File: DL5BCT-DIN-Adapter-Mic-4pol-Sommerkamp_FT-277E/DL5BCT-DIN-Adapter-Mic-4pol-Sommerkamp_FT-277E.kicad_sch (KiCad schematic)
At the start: 2 parts, among them J1 DIN-5_180degree, J2 GX16-4_Radio_Microphone-4-pol

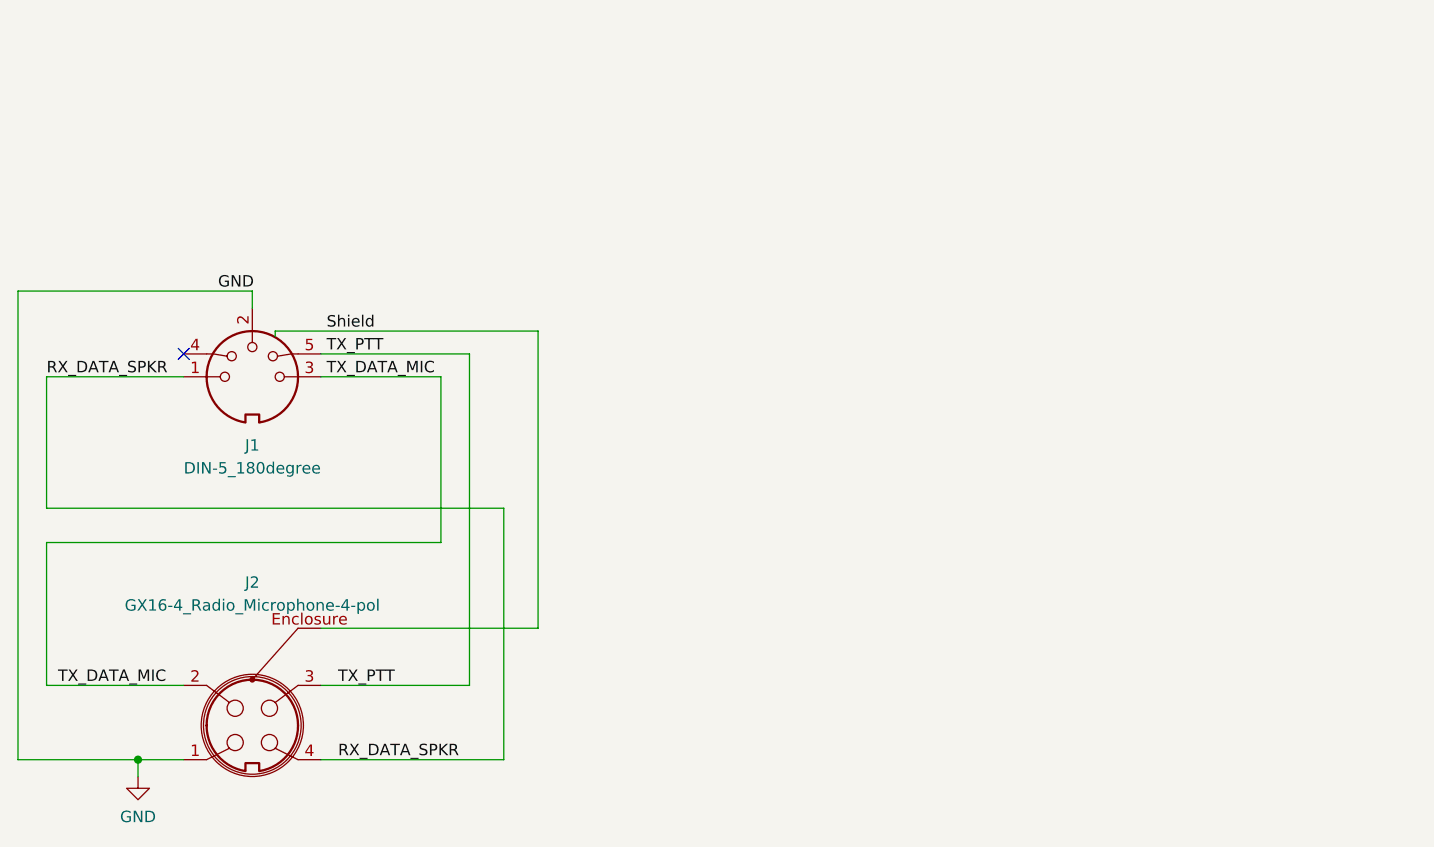
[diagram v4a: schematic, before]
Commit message: Added 'text table' with cable colour conventions. 	modified:   DL5BCT-DIN-Adapter-Mic-4pol-Sommerkamp_FT-277E/DL5BCT-DIN-Adapter-Mic-4pol-Sommerkamp_FT-277E.kicad_sch 	modified:   DL5BCT-DIN-Adapter-Mic-6pol-Kenwood_Trio_TR9000/DL5BCT-DIN-Adapter-Mic-6pol-Kenwood_Trio_TR9000.kicad_sch 	modified:   DL5BCT-DIN-Standard/DL5BCT-DIN-Standard.kicad_sch
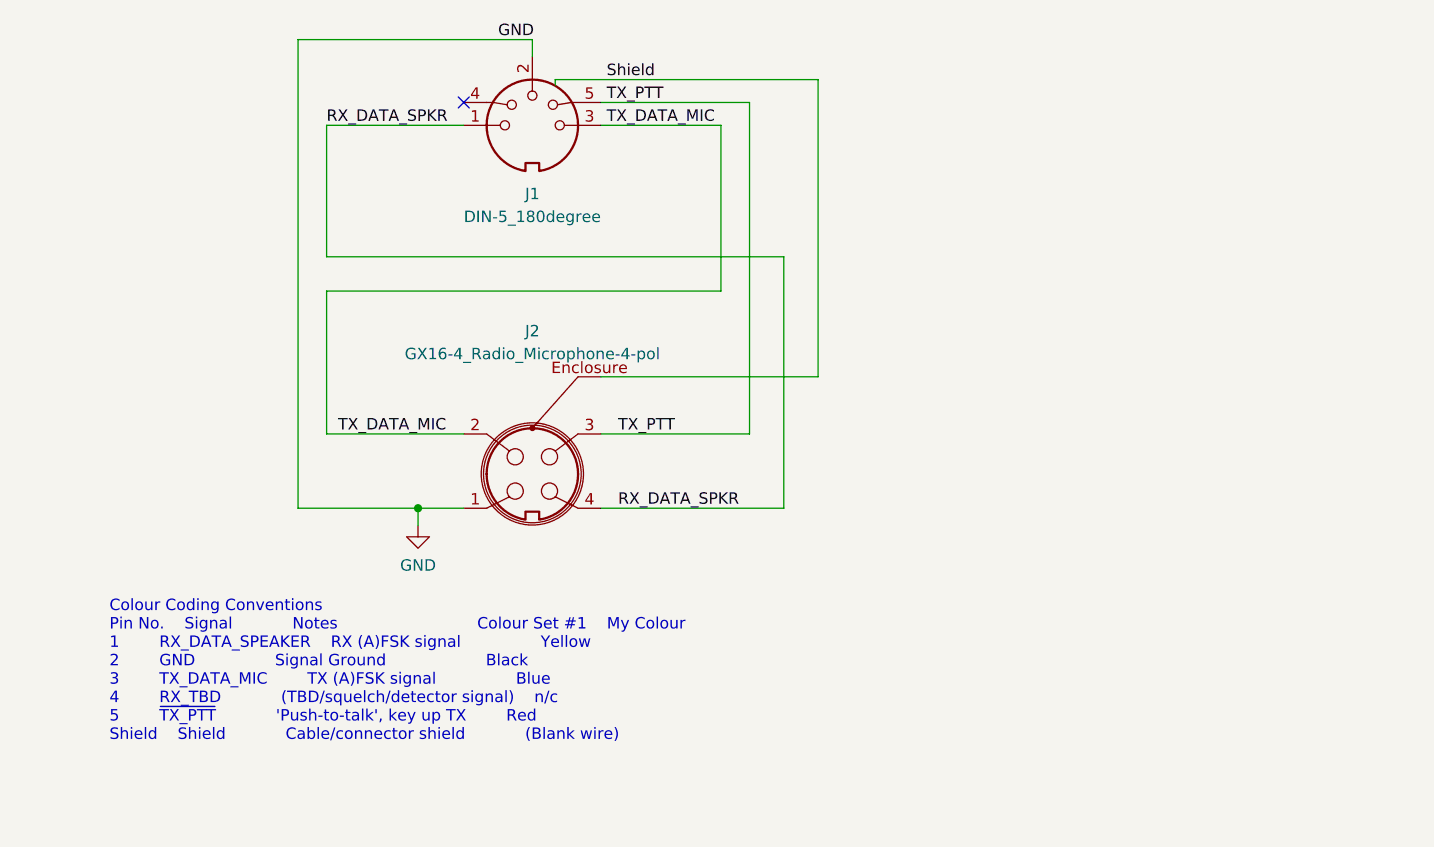
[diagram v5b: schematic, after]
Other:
- note added: "Colour Coding Conventions Pin No. Signal Notes Colour Set #1 My Colour 1 RX_DATA_SPEAKER RX (A)FSK signal Yellow 2 GND Signal Ground Black 3 TX_DATA_MIC TX (A)FSK signal Blue 4 RX_TBD (TBD/squelch/detector signal) n/c 5 ~{TX_PTT} 'Push-to-talk', key up TX Red Shield Shield Cable/connector shield (Blank wire)"
- moved on the sheet: J1, J2
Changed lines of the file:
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@@
 (kicad_sch (version 20211123) (generator eeschema)
-  (paper "A5" portrait)
+  (paper "A5")
   (title_block
     (title "Adaptor DL5BCT-DIN-Standard <--> TRX MIC 4-pol")
@@
     (comment 2 "Sommerkamp FT-277 E")
   )
-  (junction (at 62.865 100.965) (diameter 0) (color 0 0 0 0)
+  (junction (at 93.98 73.025) (diameter 0) (color 0 0 0 0)
   )
-  (no_connect (at 67.945 55.88))
-  (wire (pts (xy 52.705 73.025) (xy 52.705 58.42))
+  (no_connect (at 99.06 27.94))
+  (wire (pts (xy 83.82 45.085) (xy 83.82 30.48))
     (stroke (width 0) (type default) (color 0 0 0 0))
   )
-  (wire (pts (xy 96.52 76.835) (xy 96.52 58.42))
+  (wire (pts (xy 127.635 48.895) (xy 127.635 30.48))
     (stroke (width 0) (type default) (color 0 0 0 0))
   )
-  (wire (pts (xy 62.865 100.965) (xy 67.945 100.965))
+  (wire (pts (xy 93.98 73.025) (xy 99.06 73.025))
     (stroke (width 0) (type default) (color 0 0 0 0))
   )
-  (wire (pts (xy 78.105 53.34) (xy 78.105 53.975))
+  (wire (pts (xy 109.22 25.4) (xy 109.22 26.035))
     (stroke (width 0) (type default) (color 0 0 0 0))
   )
-  (wire (pts (xy 52.705 92.71) (xy 52.705 76.835))
+  (wire (pts (xy 83.82 64.77) (xy 83.82 48.895))
     (stroke (width 0) (type default) (color 0 0 0 0))
   )
-  (wire (pts (xy 52.705 76.835) (xy 96.52 76.835))
+  (wire (pts (xy 83.82 48.895) (xy 127.635 48.895))
     (stroke (width 0) (type default) (color 0 0 0 0))
   )
-  (wire (pts (xy 75.565 48.895) (xy 75.565 50.8))
+  (wire (pts (xy 106.68 20.955) (xy 106.68 22.86))
     (stroke (width 0) (type default) (color 0 0 0 0))
   )
-  (wire (pts (xy 83.185 86.36) (xy 107.315 86.36))
+  (wire (pts (xy 114.3 58.42) (xy 138.43 58.42))
     (stroke (width 0) (type default) (color 0 0 0 0))
   )
-  (wire (pts (xy 103.505 73.025) (xy 52.705 73.025))
+  (wire (pts (xy 134.62 45.085) (xy 83.82 45.085))
     (stroke (width 0) (type default) (color 0 0 0 0))
   )
-  (wire (pts (xy 107.315 86.36) (xy 107.315 53.34))
+  (wire (pts (xy 138.43 58.42) (xy 138.43 25.4))
     (stroke (width 0) (type default) (color 0 0 0 0))
   )
-  (wire (pts (xy 99.695 55.88) (xy 83.185 55.88))
+  (wire (pts (xy 130.81 27.94) (xy 114.3 27.94))
     (stroke (width 0) (type default) (color 0 0 0 0))
   )
-  (wire (pts (xy 49.53 100.965) (xy 62.865 100.965))
+  (wire (pts (xy 80.645 73.025) (xy 93.98 73.025))
     (stroke (width 0) (type default) (color 0 0 0 0))
   )
-  (wire (pts (xy 83.185 92.71) (xy 99.695 92.71))
+  (wire (pts (xy 114.3 64.77) (xy 130.81 64.77))
     (stroke (width 0) (type default) (color 0 0 0 0))
   )
-  (wire (pts (xy 83.185 100.965) (xy 103.505 100.965))
+  (wire (pts (xy 114.3 73.025) (xy 134.62 73.025))
     (stroke (width 0) (type default) (color 0 0 0 0))
   )
-  (wire (pts (xy 52.705 92.71) (xy 67.945 92.71))
+  (wire (pts (xy 83.82 64.77) (xy 99.06 64.77))
     (stroke (width 0) (type default) (color 0 0 0 0))
   )
-  (wire (pts (xy 49.53 48.895) (xy 49.53 100.965))
+  (wire (pts (xy 80.645 20.955) (xy 80.645 73.025))
     (stroke (width 0) (type default) (color 0 0 0 0))
   )
-  (wire (pts (xy 49.53 48.895) (xy 75.565 48.895))
+  (wire (pts (xy 80.645 20.955) (xy 106.68 20.955))
     (stroke (width 0) (type default) (color 0 0 0 0))
   )
-  (wire (pts (xy 107.315 53.34) (xy 78.105 53.34))
+  (wire (pts (xy 138.43 25.4) (xy 109.22 25.4))
     (stroke (width 0) (type default) (color 0 0 0 0))
   )
-  (wire (pts (xy 96.52 58.42) (xy 83.185 58.42))
+  (wire (pts (xy 127.635 30.48) (xy 114.3 30.48))
     (stroke (width 0) (type default) (color 0 0 0 0))
   )
-  (wire (pts (xy 62.865 100.965) (xy 62.865 102.87))
+  (wire (pts (xy 93.98 73.025) (xy 93.98 74.93))
     (stroke (width 0) (type default) (color 0 0 0 0))
   )
-  (wire (pts (xy 52.705 58.42) (xy 67.945 58.42))
+  (wire (pts (xy 83.82 30.48) (xy 99.06 30.48))
     (stroke (width 0) (type default) (color 0 0 0 0))
   )
-  (wire (pts (xy 103.505 100.965) (xy 103.505 73.025))
+  (wire (pts (xy 134.62 73.025) (xy 134.62 45.085))
     (stroke (width 0) (type default) (color 0 0 0 0))
   )
-  (wire (pts (xy 99.695 92.71) (xy 99.695 55.88))
+  (wire (pts (xy 130.81 64.77) (xy 130.81 27.94))
     (stroke (width 0) (type default) (color 0 0 0 0))
   )
-  (label "Shield" (at 83.82 53.34 0)
+  (text "Colour Coding Conventions\nPin No.	Signal			Notes							Colour Set #1	My Colour\n1		RX_DATA_SPEAKER	RX (A)FSK signal				Yellow			\n2		GND				Signal Ground					Black			\n3		TX_DATA_MIC		TX (A)FSK signal				Blue			\n4		RX_TBD			(TBD/squelch/detector signal)	n/c				\n5		~{TX_PTT}			'Push-to-talk', key up TX		Red				\nShield	Shield			Cable/connector shield			(Blank wire)	"
+    (at 59.69 99.06 0)
     (effects (font (size 1.27 1.27)) (justify left bottom))
   )
-  (label "TX_PTT" (at 85.09 92.71 0)
+  (label "Shield" (at 114.935 25.4 0)
     (effects (font (size 1.27 1.27)) (justify left bottom))
   )
-  (label "TX_DATA_MIC" (at 53.975 92.71 0)
+  (label "TX_PTT" (at 116.205 64.77 0)
     (effects (font (size 1.27 1.27)) (justify left bottom))
   )
-  (label "TX_PTT" (at 83.82 55.88 0)
+  (label "TX_DATA_MIC" (at 85.09 64.77 0)
     (effects (font (size 1.27 1.27)) (justify left bottom))
   )
-  (label "TX_DATA_MIC" (at 83.82 58.42 0)
+  (label "TX_PTT" (at 114.935 27.94 0)
     (effects (font (size 1.27 1.27)) (justify left bottom))
   )
-  (label "RX_DATA_SPKR" (at 52.705 58.42 0)
+  (label "TX_DATA_MIC" (at 114.935 30.48 0)
     (effects (font (size 1.27 1.27)) (justify left bottom))
   )
-  (label "RX_DATA_SPKR" (at 85.09 100.965 0)
+  (label "RX_DATA_SPKR" (at 83.82 30.48 0)
     (effects (font (size 1.27 1.27)) (justify left bottom))
   )
-  (label "GND" (at 71.755 48.895 0)
+  (label "RX_DATA_SPKR" (at 116.205 73.025 0)
     (effects (font (size 1.27 1.27)) (justify left bottom))
   )
-  (symbol (lib_id "Connector:DIN-5_180degree") (at 75.565 58.42 0) (unit 1)
+  (label "GND" (at 102.87 20.955 0)
+    (effects (font (size 1.27 1.27)) (justify left bottom))
+  )
+  (symbol (lib_id "Connector:DIN-5_180degree") (at 106.68 30.48 0) (unit 1)
     (in_bom yes) (on_board yes) (fields_autoplaced)
-    (property "Reference" "J1" (id 0) (at 75.5651 66.04 0))
-    (property "Value" "DIN-5_180degree" (id 1) (at 75.5651 68.58 0))
-    (property "Footprint" "" (id 2) (at 75.565 58.42 0)
+    (property "Reference" "J1" (id 0) (at 106.6801 38.1 0))
+    (property "Value" "DIN-5_180degree" (id 1) (at 106.6801 40.64 0))
+    (property "Footprint" "" (id 2) (at 106.68 30.48 0)
       (effects (font (size 1.27 1.27)) hide)
     )
-    (property "Datasheet" "http://www.mouser.com/ds/2/18/40_c091_abd_e-75918.pdf" (id 3) (at 75.565 58.42 0)
+    (property "Datasheet" "http://www.mouser.com/ds/2/18/40_c091_abd_e-75918.pdf" (id 3) (at 106.68 30.48 0)
       (effects (font (size 1.27 1.27)) hide)
     )
@@
     (pin "5")
   )
-  (symbol (lib_id "power:GND") (at 62.865 102.87 0) (unit 1)
+  (symbol (lib_id "power:GND") (at 93.98 74.93 0) (unit 1)
     (in_bom yes) (on_board yes) (fields_autoplaced)
-    (property "Reference" "#PWR01" (id 0) (at 62.865 109.22 0)
+    (property "Reference" "#PWR01" (id 0) (at 93.98 81.28 0)
       (effects (font (size 1.27 1.27)) hide)
     )
-    (property "Value" "GND" (id 1) (at 62.865 107.315 0))
-    (property "Footprint" "" (id 2) (at 62.865 102.87 0)
+    (property "Value" "GND" (id 1) (at 93.98 79.375 0))
+    (property "Footprint" "" (id 2) (at 93.98 74.93 0)
       (effects (font (size 1.27 1.27)) hide)
     )
-    (property "Datasheet" "" (id 3) (at 62.865 102.87 0)
+    (property "Datasheet" "" (id 3) (at 93.98 74.93 0)
       (effects (font (size 1.27 1.27)) hide)
     )
     (pin "1")
   )
-  (symbol (lib_id "DL5BCT-DIN-Standard:GX16-4_Radio_Microphone-4-pol") (at 67.945 100.965 0) (unit 1)
+  (symbol (lib_id "DL5BCT-DIN-Standard:GX16-4_Radio_Microphone-4-pol") (at 99.06 73.025 0) (unit 1)
     (in_bom yes) (on_board yes) (fields_autoplaced)
-    (property "Reference" "J2" (id 0) (at 75.565 81.28 0))
-    (property "Value" "GX16-4_Radio_Microphone-4-pol" (id 1) (at 75.565 83.82 0))
-    (property "Footprint" "" (id 2) (at 75.565 97.155 0)
+    (property "Reference" "J2" (id 0) (at 106.68 53.34 0))
+    (property "Value" "GX16-4_Radio_Microphone-4-pol" (id 1) (at 106.68 55.88 0))
+    (property "Footprint" "" (id 2) (at 106.68 69.215 0)
       (effects (font (size 1.27 1.27)) hide)
     )
-    (property "Datasheet" "https://cdn-reichelt.de/documents/datenblatt/C160/M604.pdf" (id 3) (at 75.565 109.855 0)
+    (property "Datasheet" "https://cdn-reichelt.de/documents/datenblatt/C160/M604.pdf" (id 3) (at 106.68 81.915 0)
       (effects (font (size 1.27 1.27)) hide)
     )
-    (property "Datasheet2" "https://www.renhotecpro.com/wp-content/uploads/2017/04/GX-Series-Aviation-Connectors-Presentation.pdf" (id 4) (at 67.945 112.395 0)
+    (property "Datasheet2" "https://www.renhotecpro.com/wp-content/uploads/2017/04/GX-Series-Aviation-Connectors-Presentation.pdf" (id 4) (at 99.06 84.455 0)
       (effects (font (size 1.27 1.27)) hide)
     )
